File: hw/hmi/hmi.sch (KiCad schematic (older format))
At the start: 66 parts, among them J1 SWD, J2 INTERFACE, J3 GPS, J4 SSD1963_LCD, J5 USB, J6 Antenna, Q1 BC847, U1 STM32F412VETx, U2 USB6B1, U3 RFM69HW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

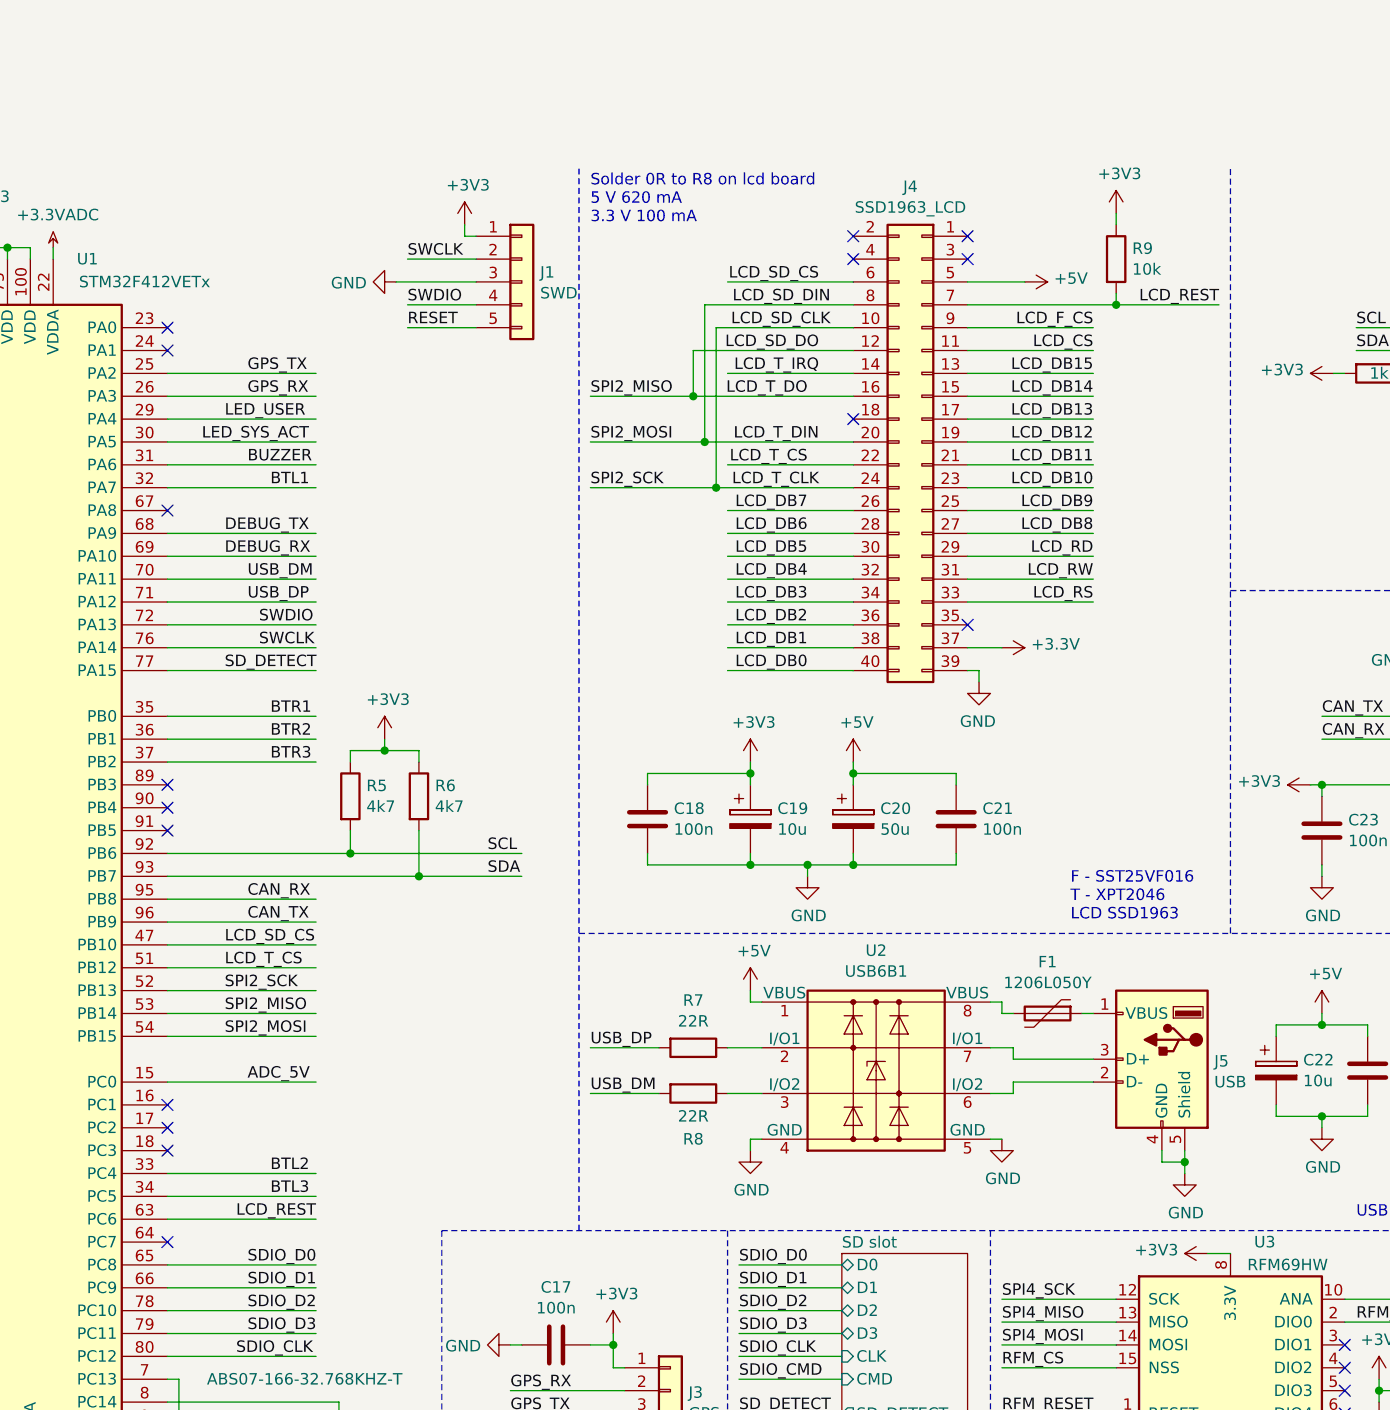
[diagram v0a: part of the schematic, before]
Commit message: Added HMI and SDU boards
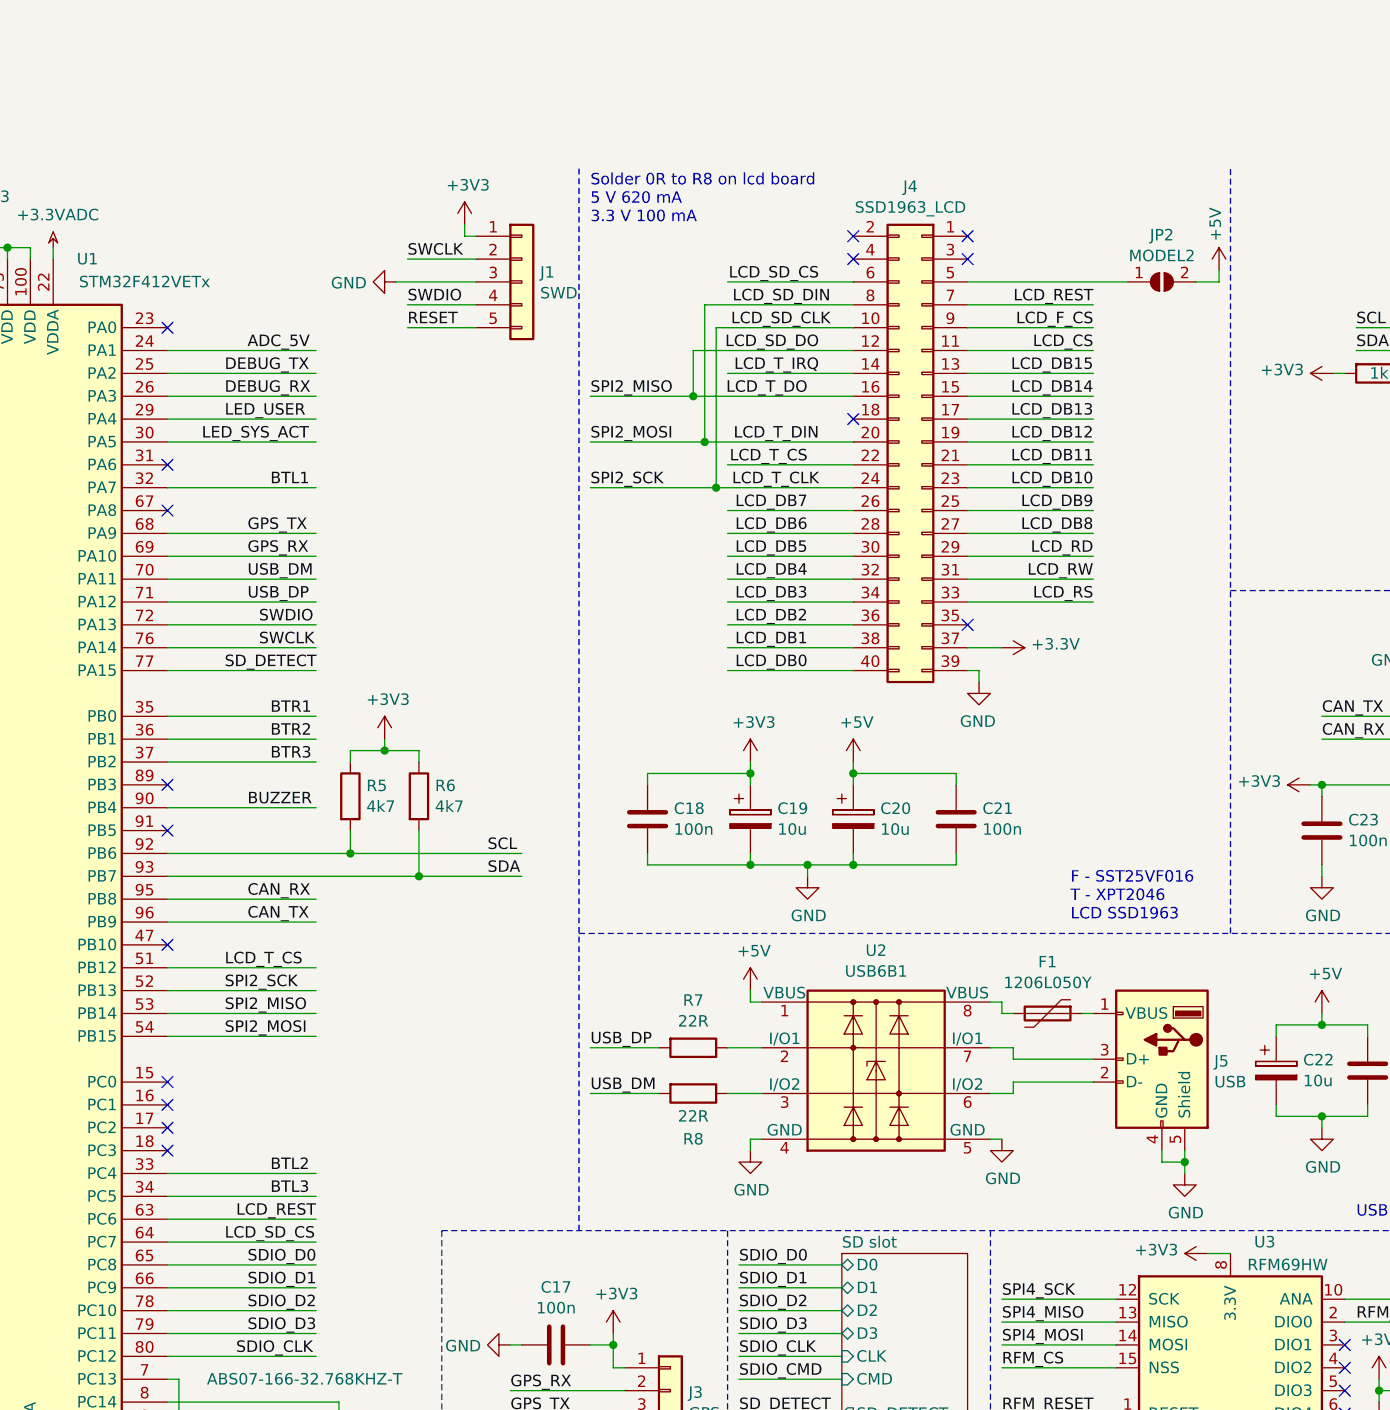
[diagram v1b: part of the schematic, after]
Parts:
- removed R9: 10k, Resistor_SMD:R_0805_2012Metric, symbol Device:R
- added JP2: MODEL2, Jumper:SolderJumper-2_P1.3mm_Open_TrianglePad1.0x1.5mm, symbol Jumper:SolderJumper_2_Open
- C20: value 50u -> 10u; footprint Capacitor_SMD:CP_Elec_6.3x7.7 -> Capacitor_SMD:C_0805_2012Metric
- J1: footprint Connector_PinHeader_2.54mm:PinHeader_1x05_P2.54mm_Vertical -> Connector_PinHeader_2.54mm:PinHeader_1x05_P2.54mm_Horizontal
- J2: footprint Connector_Dsub:DSUB-9_Female_Horizontal_P2.77x2.84mm_EdgePinOffset9.90mm_Housed_MountingHolesOffset11.32mm -> Connector_Dsub:DSUB-9_Female_Vertical_P2.77x2.84mm_MountingHoles
- J5: footprint Connector_USB:USB_B_TE_5787834_Vertical -> Connector_USB:USB_A_Molex_105057_Vertical
- J6: footprint Connector_Coaxial:SMA_Amphenol_132289_EdgeMount -> Connector_Coaxial:SMA_Amphenol_132134-11_Vertical
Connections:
- wire segments 417 -> 416
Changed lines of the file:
@@
 L power:+5V #PWR0102
 U 1 1 5BC43D59
-P 7500 1000
-F 0 "#PWR0102" H 7500 850 50  0001 C CNN
-F 1 "+5V" V 7515 1128 50  0000 L CNN
-F 2 "" H 7500 1000 50  0001 C CNN
-F 3 "" H 7500 1000 50  0001 C CNN
-	1    7500 1000
-	0    1    -1   0
-$EndComp
-Wire Wire Line
-	7500 1000 7250 1000
-Wire Wire Line
-	7250 1100 7900 1100
-Text Label 8350 1100 2    50   ~ 0
+P 8350 950
+F 0 "#PWR0102" H 8350 800 50  0001 C CNN
+F 1 "+5V" V 8365 1078 50  0000 L CNN
+F 2 "" H 8350 950 50  0001 C CNN
+F 3 "" H 8350 950 50  0001 C CNN
+	1    8350 950
+	-1   0    0    -1
+$EndComp
+Text Label 7800 1100 2    50   ~ 0
 LCD_REST
 Wire Wire Line
@@
 F 0 "J2" H 5800 6650 50  0000 L CNN
 F 1 "INTERFACE" V 5900 6950 50  0000 L CNN
-F 2 "Connector_Dsub:DSUB-9_Female_Horizontal_P2.77x2.84mm_EdgePinOffset9.90mm_Housed_MountingHolesOffset11.32mm" H 5700 7150 50  0001 C CNN
+F 2 "Connector_Dsub:DSUB-9_Female_Vertical_P2.77x2.84mm_MountingHoles" H 5700 7150 50  0001 C CNN
 F 3 " ~" H 5700 7150 50  0001 C CNN
 	1    5700 7150
@@
 $EndComp
 Wire Wire Line
-	3750 2200 4400 2200
-Text Label 4000 2200 0    50   ~ 0
+	3750 1500 4400 1500
+Text Label 4000 1500 0    50   ~ 0
 DEBUG_RX
 Wire Wire Line
-	3750 2100 4400 2100
-Text Label 4000 2100 0    50   ~ 0
+	3750 1400 4400 1400
+Text Label 4000 1400 0    50   ~ 0
 DEBUG_TX
 Wire Wire Line
@@
 $EndComp
 Wire Wire Line
-	3750 1400 4400 1400
-Text Label 4100 1400 0    50   ~ 0
+	3750 2100 4400 2100
+Text Label 4100 2100 0    50   ~ 0
 GPS_TX
 Wire Wire Line
-	3750 1500 4400 1500
-Text Label 4100 1500 0    50   ~ 0
+	3750 2200 4400 2200
+Text Label 4100 2200 0    50   ~ 0
 GPS_RX
 Text Label 4150 2600 0    50   ~ 0
@@
 F 0 "J1" H 5380 1042 50  0000 L CNN
 F 1 "SWD" H 5380 951 50  0000 L CNN
-F 2 "Connector_PinHeader_2.54mm:PinHeader_1x05_P2.54mm_Vertical" H 5300 1000 50  0001 C CNN
+F 2 "Connector_PinHeader_2.54mm:PinHeader_1x05_P2.54mm_Horizontal" H 5300 1000 50  0001 C CNN
 F 3 "~" H 5300 1000 50  0001 C CNN
 	1    5300 1000
@@
 F 0 "J5" H 7871 4391 50  0000 R CNN
 F 1 "USB" H 7871 4300 50  0000 R CNN
-F 2 "Connector_USB:USB_B_TE_5787834_Vertical" H 8250 4350 50  0001 C CNN
+F 2 "Connector_USB:USB_A_Molex_105057_Vertical" H 8250 4350 50  0001 C CNN
 F 3 " ~" H 8250 4350 50  0001 C CNN
 	1    8100 4400
@@
 	6150 1900 6750 1900
 Wire Wire Line
-	3750 3900 4400 3900
-Text Label 4000 3900 0    50   ~ 0
+	3750 5200 4400 5200
+Text Label 4000 5200 0    50   ~ 0
 LCD_SD_CS
 Wire Wire Line
@@
 Text Label 1350 5700 0    50   ~ 0
 LCD_F_CS
-$Comp
-L Device:R R9
-U 1 1 5CA6233D
-P 7900 900
-F 0 "R9" H 7970 946 50  0000 L CNN
-F 1 "10k" H 7970 855 50  0000 L CNN
-F 2 "Resistor_SMD:R_0805_2012Metric" V 7830 900 50  0001 C CNN
-F 3 "~" H 7900 900 50  0001 C CNN
-	1    7900 900
-	1    0    0    -1
-$EndComp
-$Comp
-L power:+3V3 #PWR0131
-U 1 1 5CA62430
-P 7900 700
-F 0 "#PWR0131" H 7900 550 50  0001 C CNN
-F 1 "+3V3" H 7915 873 50  0000 C CNN
-F 2 "" H 7900 700 50  0001 C CNN
-F 3 "" H 7900 700 50  0001 C CNN
-	1    7900 700
-	1    0    0    -1
-$EndComp
-Wire Wire Line
-	7900 700  7900 750
-Wire Wire Line
-	7900 1050 7900 1100
-Connection ~ 7900 1100
-Wire Wire Line
-	7900 1100 8350 1100
 $Comp
 L Device:CP C20
@@
 P 6750 3350
 F 0 "C20" H 6868 3396 50  0000 L CNN
-F 1 "50u" H 6868 3305 50  0000 L CNN
-F 2 "Capacitor_SMD:CP_Elec_6.3x7.7" H 6788 3200 50  0001 C CNN
+F 1 "10u" H 6868 3305 50  0000 L CNN
+F 2 "Capacitor_SMD:C_0805_2012Metric" H 6788 3200 50  0001 C CNN
 F 3 "~" H 6750 3350 50  0001 C CNN
 	1    6750 3350
@@
 F - SST25VF016\nT - XPT2046\nLCD SSD1963
 Wire Wire Line
-	3750 4500 4400 4500
-Text Label 4100 4500 0    50   ~ 0
+	3750 1300 4400 1300
+Text Label 4100 1300 0    50   ~ 0
 ADC_5V
 Text Notes 10900 5100 0    50   ~ 0
@@
 	8400 3850 8400 500
 Wire Wire Line
-	3750 1800 4400 1800
-Text Label 4100 1800 0    50   ~ 0
+	3750 3300 4400 3300
+Text Label 4100 3300 0    50   ~ 0
 BUZZER
 Wire Notes Line
@@
 Text Label 4000 1600 0    50   ~ 0
 LED_USER
-NoConn ~ 3750 5200
+NoConn ~ 3750 3900
 NoConn ~ 3750 4700
 NoConn ~ 3750 4600
 NoConn ~ 3750 3400
-NoConn ~ 3750 3300
+NoConn ~ 3750 1800
 NoConn ~ 3750 2000
-NoConn ~ 3750 1300
+NoConn ~ 3750 4500
 NoConn ~ 3750 1200
 NoConn ~ 1950 4800
@@
 F 0 "J6" H 9600 5426 50  0000 L CNN
 F 1 "Antenna" H 9300 5600 50  0000 L CNN
-F 2 "Connector_Coaxial:SMA_Amphenol_132289_EdgeMount" H 9500 5450 50  0001 C CNN
+F 2 "Connector_Coaxial:SMA_Amphenol_132134-11_Vertical" H 9500 5450 50  0001 C CNN
 F 3 " ~" H 9500 5450 50  0001 C CNN
 	1    9500 5450
@@
 Text Notes 9650 -300 0    50   ~ 0
 3.3V z lineárního stabilizátoru
+$Comp
+L Jumper:SolderJumper_2_Open JP2
+U 1 1 5C167EE9
+P 8100 1000
+F 0 "JP2" H 8100 1205 50  0000 C CNN
+F 1 "MODEL2" H 8100 1114 50  0000 C CNN
+F 2 "Jumper:SolderJumper-2_P1.3mm_Open_TrianglePad1.0x1.5mm" H 8100 1000 50  0001 C CNN
+F 3 "~" H 8100 1000 50  0001 C CNN
+	1    8100 1000
+	1    0    0    -1
+$EndComp
+Wire Wire Line
+	7950 1000 7250 1000
+Wire Wire Line
+	8350 950  8350 1000
+Wire Wire Line
+	8350 1000 8250 1000
+Wire Wire Line
+	7250 1100 7800 1100
 $EndSCHEMATC

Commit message: Updated power supply in HMI
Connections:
- net labels added: +3.3VP
- net labels removed: +3.3V
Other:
- note added: "Solder 0R to R8 on lcd board\n5 V 620 mA\n3.3 V 100 mA / 450 mA"
- note removed: "Solder 0R to R8 on lcd board\n5 V 620 mA\n3.3 V 100 mA"
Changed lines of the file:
@@
 Text Label 7800 1500 2    50   ~ 0
 LCD_DB14
-$Comp
-L power:+3.3V #PWR0103
-U 1 1 5BC48095
-P 7400 2600
-F 0 "#PWR0103" H 7400 2450 50  0001 C CNN
-F 1 "+3.3V" V 7415 2728 50  0000 L CNN
-F 2 "" H 7400 2600 50  0001 C CNN
-F 3 "" H 7400 2600 50  0001 C CNN
-	1    7400 2600
-	0    1    -1   0
-$EndComp
 Wire Wire Line
 	7400 2600 7250 2600
@@
 SD_DETECT
 Text Notes 5600 750  0    50   ~ 0
-Solder 0R to R8 on lcd board\n5 V 620 mA\n3.3 V 100 mA
+Solder 0R to R8 on lcd board\n5 V 620 mA\n3.3 V 100 mA / 450 mA
 Wire Wire Line
 	5600 1900 6150 1900
@@
 Wire Wire Line
 	6300 3150 6300 3200
-$Comp
-L power:+3V3 #PWR0133
-U 1 1 5CB494FE
-P 6300 3100
-F 0 "#PWR0133" H 6300 2950 50  0001 C CNN
-F 1 "+3V3" H 6315 3273 50  0000 C CNN
-F 2 "" H 6300 3100 50  0001 C CNN
-F 3 "" H 6300 3100 50  0001 C CNN
-	1    6300 3100
-	1    0    0    -1
-$EndComp
 Wire Wire Line
 	6300 3100 6300 3150
@@
 Wire Wire Line
 	7250 1100 7800 1100
+$Comp
+L power:+3.3VP #PWR0103
+U 1 1 5C175F16
+P 7400 2600
+F 0 "#PWR0103" H 7550 2550 50  0001 C CNN
+F 1 "+3.3VP" V 7420 2698 50  0000 L CNN
+F 2 "" H 7400 2600 50  0001 C CNN
+F 3 "" H 7400 2600 50  0001 C CNN
+	1    7400 2600
+	0    1    1    0
+$EndComp
+$Comp
+L power:+3.3VP #PWR?
+U 1 1 5C17B1F4
+P 6300 3100
+F 0 "#PWR?" H 6450 3050 50  0001 C CNN
+F 1 "+3.3VP" H 6320 3243 50  0000 C CNN
+F 2 "" H 6300 3100 50  0001 C CNN
+F 3 "" H 6300 3100 50  0001 C CNN
+	1    6300 3100
+	1    0    0    -1
+$EndComp
 $EndSCHEMATC

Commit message: Added pressure sensor to hmi
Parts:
- removed C17, C29, C30: 100n, Capacitor_SMD:C_0805_2012Metric, symbol Device:C
- removed J3: GPS, Connector_Molex:Molex_KK-254_AE-6410-04A_1x04_P2.54mm_Vertical, symbol Connector_Generic:Conn_01x04
- removed R10: 1k, Resistor_SMD:R_0805_2012Metric, symbol Device:R
- removed U5: LSM303C, Package_LGA:LGA-12_2x2mm_P0.5mm, symbol Sensor_Motion:LSM303C
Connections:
- net labels added: BME_CS
- wire segments 416 -> 395
- no-connect marks 27 -> 23
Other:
- note added: "Sensors"
- note removed: "3.3V z lineárního stabilizátoru"
- note removed: "Accelerometer"
- note removed: "GPS"
- moved on the sheet: C23, C27, JP1, R13, U4
